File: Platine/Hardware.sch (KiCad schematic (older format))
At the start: 163 parts, among them J1 Barrel_Jack_Switch, J2 Screw_Terminal_01x02, J3 USB_B, Q1 BCX19, Q2 BCX19, SW1 SW_Soft_Reset, SW2 SW_Hard_Reset, SW3 SW_Flash, U1 ESP32-WROOM-32D, U2 ZLDO1117_SOT223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

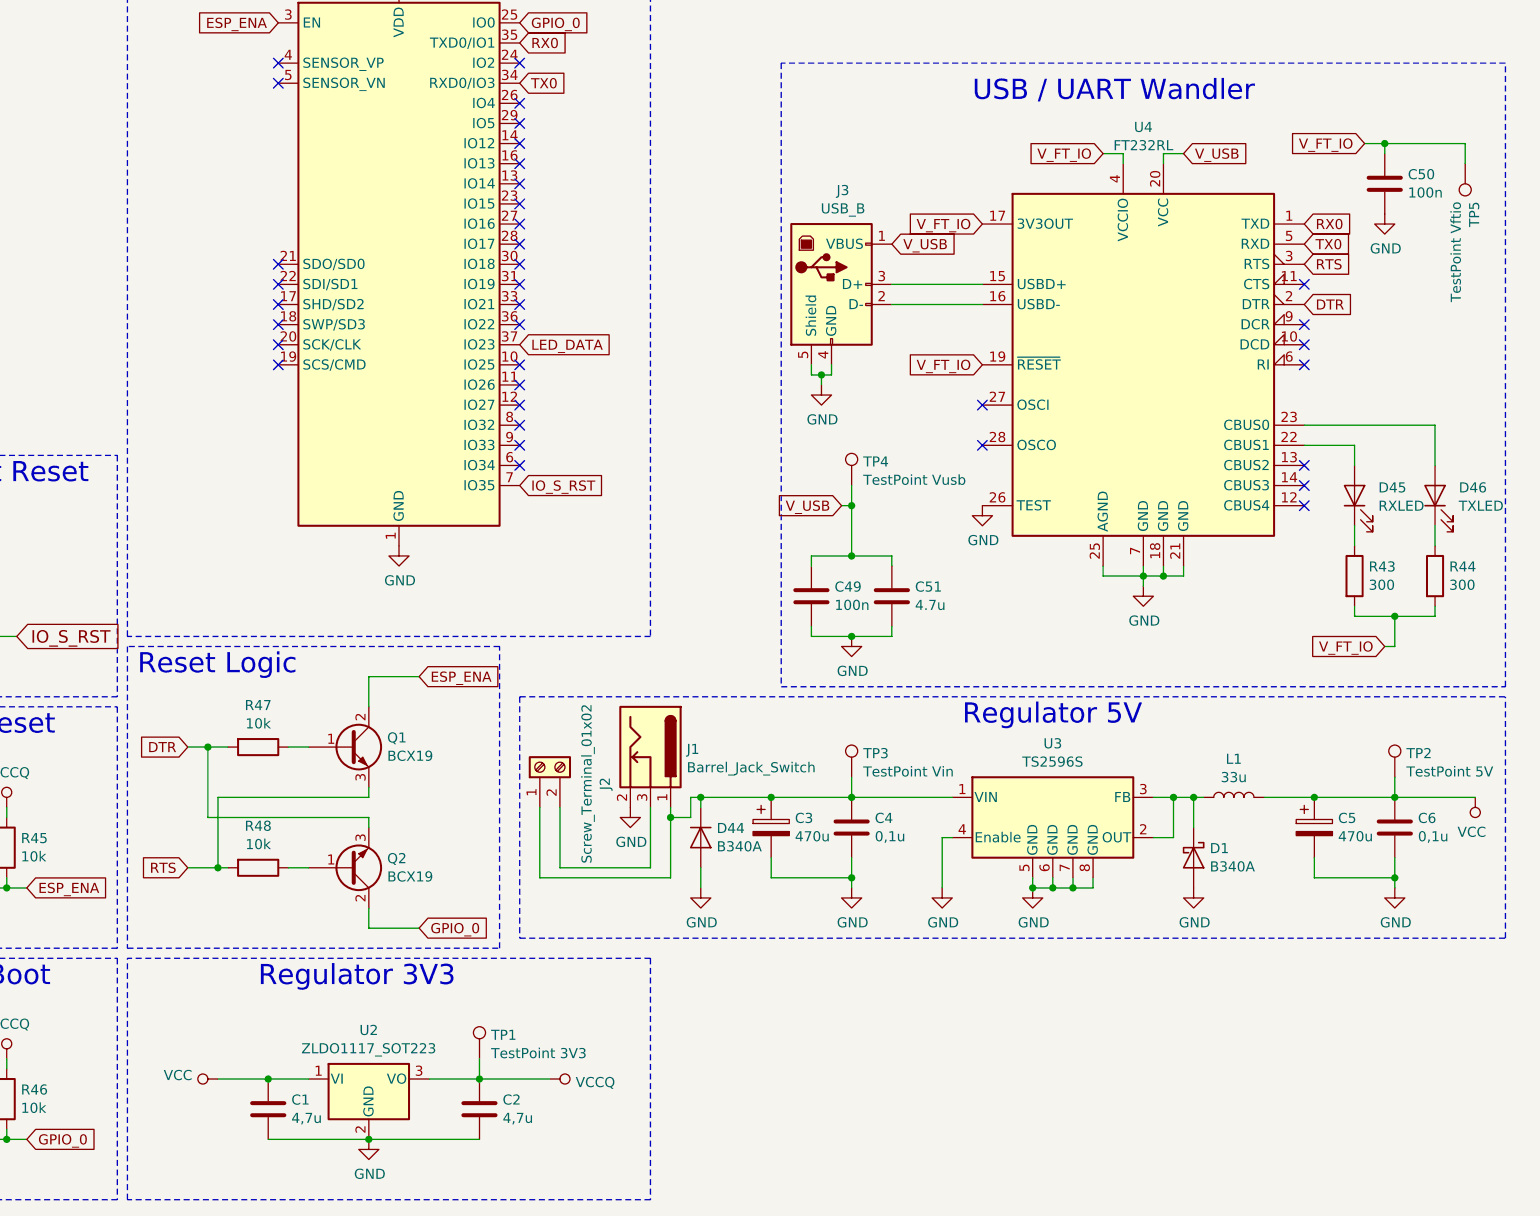
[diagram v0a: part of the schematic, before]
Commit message: Added urgent features requested by client Added power LED Added option to supply complete PCB via USB port
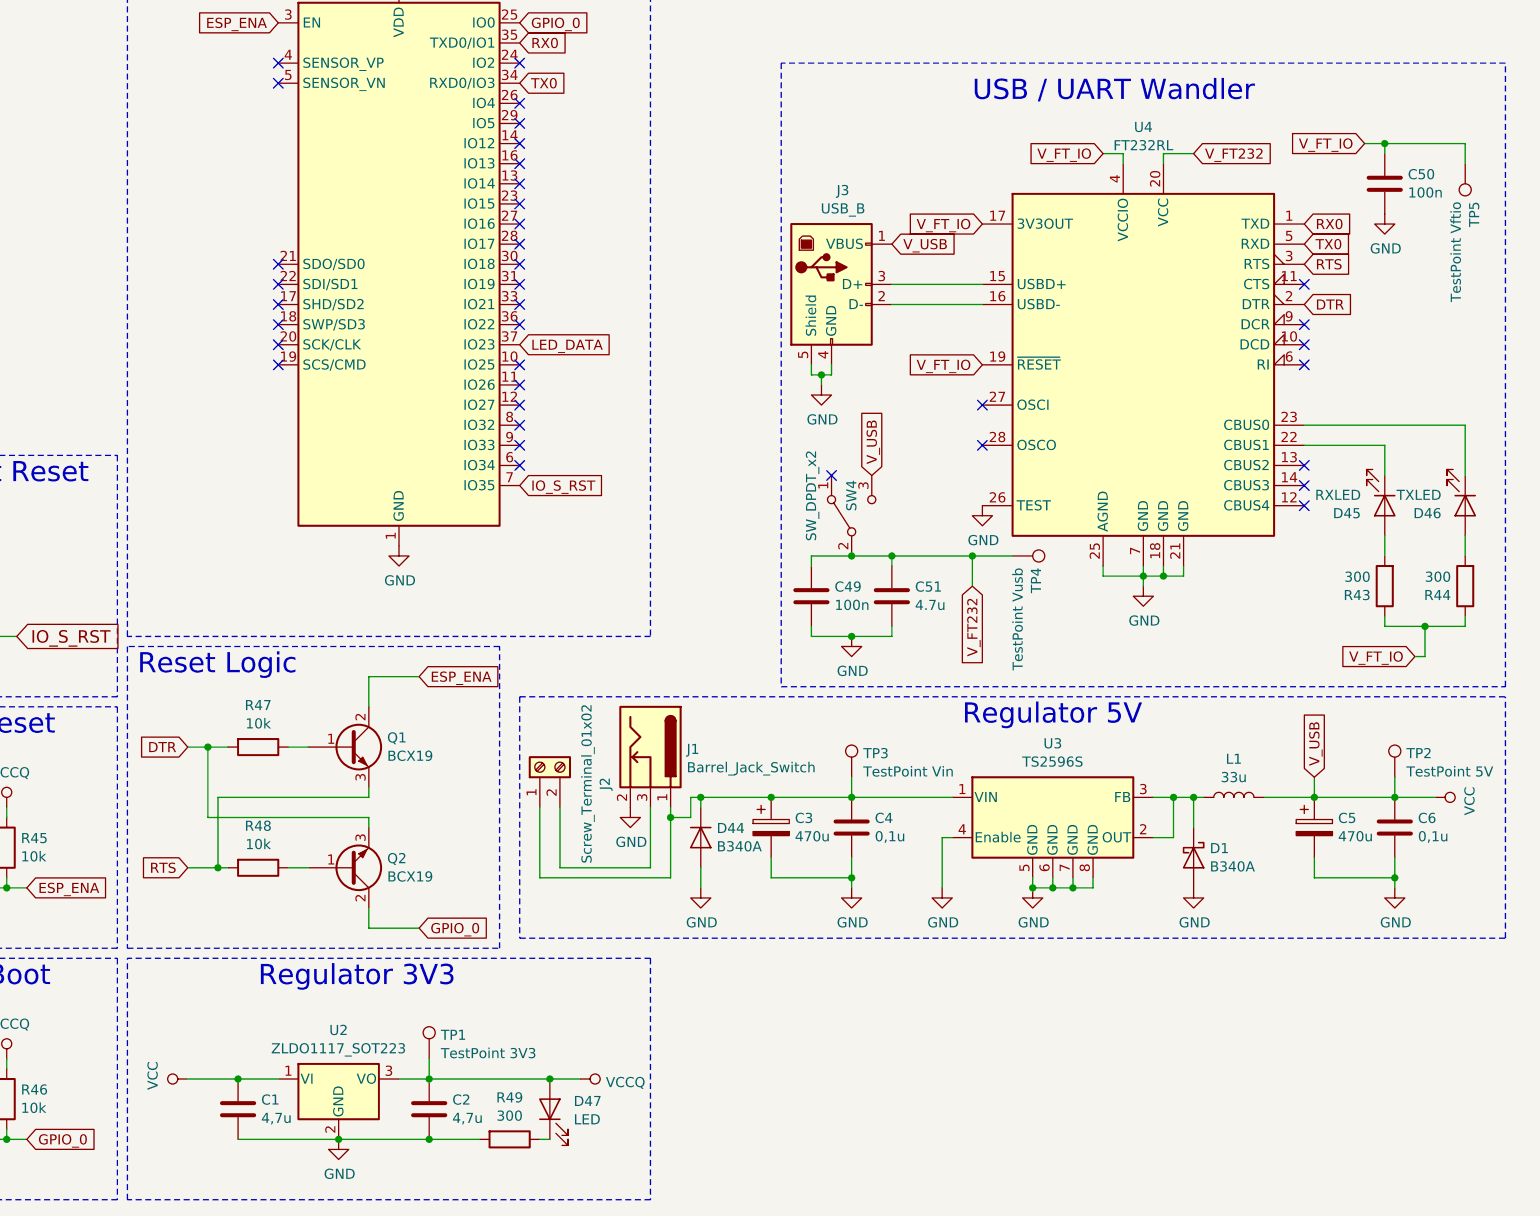
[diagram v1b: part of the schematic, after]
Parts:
- added D47: LED, Diode_SMD:D_0805_2012Metric_Pad1.15x1.40mm_HandSolder, symbol Device:LED
- added R49: 300, Resistor_SMD:R_0805_2012Metric_Pad1.15x1.40mm_HandSolder, symbol Device:R
- added SW4: SW_DPDT_x2, Custom_Footprints:Switch, symbol Switch:SW_SPDT
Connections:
- net GND: now also R49.2
- net VCC: now also J3.1 (VBUS), SW4.3 (C)
- net VCCQ: now also D47.2 (A)
- net V_FT_IO: now also R43.1, R44.1; no longer R43.2, R44.2
- net at U4.22 (CBUS1): now also D45.1 (K); no longer D45.2 (A)
- net at U4.23 (CBUS0): now also D46.1 (K); no longer D46.2 (A)
- net V_USB renamed V_FT232
- net V_FT232: now also SW4.2 (B); no longer J3.1 (VBUS)
- new net: D47.1 (K), R49.1
- new net: D45.2 (A), R43.2
- new net: D46.2 (A), R44.2
- no-connect marks 37 -> 38
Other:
- moved on the sheet: C1, C2, D45, D46, R43, R44, TP1, TP4, U2

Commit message: Production readiness Improved reverse USB powerprotection Added part orderlist
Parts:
- added Q3: NDS0610, Package_TO_SOT_SMD:SOT-23, symbol Transistor_FET:VP0610T
- added R50, R51: 10k, Resistor_SMD:R_0805_2012Metric_Pad1.15x1.40mm_HandSolder, symbol Device:R
- added U5: OP07, Package_SO:SO-8_5.3x6.2mm_P1.27mm, symbol Amplifier_Operational:OP07
- D47: footprint Diode_SMD:D_0805_2012Metric_Pad1.15x1.40mm_HandSolder -> LED_SMD:LED_0805_2012Metric_Pad1.15x1.40mm_HandSolder
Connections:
- net GND: now also R51.2, U5.4 (V-)
- net VCC: now also Q3.2 (S), U5.7 (V+); no longer J3.1 (VBUS), SW4.3 (C)
- net VCCQ: now also U5.2 (-)
- net V_IN: now reaches C3.1, C4.1, D44.1 (K), J1.1, J2.1 (Pin_1), TP3.1, U3.1 (VIN)
- net V_IN: now also R50.1
- new net: R50.2, R51.1, U5.3 (+)
- new net: Q3.1 (G), U5.6
- new net V_USB: J3.1 (VBUS), Q3.3 (D), SW4.3 (C)
- no-connect marks 38 -> 40
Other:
- note added: "USB power protection"
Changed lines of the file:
@@
 	1    0    0    -1
 $EndComp
-Wire Wire Line
-	12950 6650 13400 6650
-Wire Wire Line
-	12950 6750 13400 6750
 Text GLabel 15000 6450 2    50   Input ~ 0
 TX0
@@
 Text GLabel 12950 6450 2    50   Input ~ 0
 V_USB
-Text GLabel 14450 6000 2    50   Input ~ 0
-V_FT232
 Wire Wire Line
 	14300 6000 14300 6050
@@
 F 0 "D47" V 11289 10632 50  0000 R CNN
 F 1 "LED" V 11198 10632 50  0000 R CNN
-F 2 "Diode_SMD:D_0805_2012Metric_Pad1.15x1.40mm_HandSolder" H 11250 10750 50  0001 C CNN
+F 2 "LED_SMD:LED_0805_2012Metric_Pad1.15x1.40mm_HandSolder" H 11250 10750 50  0001 C CNN
 F 3 "https://cdn-reichelt.de/documents/datenblatt/A500/17_21SYGC_S530_E2_TR8_ENG_DATASHEET.pdf" H 11250 10750 50  0001 C CNN
 	1    11250 10750
@@
 	0    -1   -1   0
 $EndComp
-Wire Wire Line
-	15050 9200 15050 9100
-Text GLabel 15050 9100 1    50   Input ~ 0
+NoConn ~ 14150 4950
+NoConn ~ 14250 4950
+Text GLabel 11450 9750 2    50   Input ~ 0
+V_IN
+Wire Wire Line
+	11450 9750 11200 9750
+Wire Wire Line
+	11200 9750 11200 9600
+Connection ~ 11200 9600
+Text GLabel 13350 3950 0    50   Input ~ 0
+V_IN
+$Comp
+L Device:R R50
+U 1 1 6007B0D4
+P 13500 4350
+F 0 "R50" H 13570 4396 50  0000 L CNN
+F 1 "10k" H 13570 4305 50  0000 L CNN
+F 2 "Resistor_SMD:R_0805_2012Metric_Pad1.15x1.40mm_HandSolder" V 13430 4350 50  0001 C CNN
+F 3 "~" H 13500 4350 50  0001 C CNN
+	1    13500 4350
+	1    0    0    -1
+$EndComp
+$Comp
+L Device:R R51
+U 1 1 6007C91D
+P 13500 4750
+F 0 "R51" H 13570 4796 50  0000 L CNN
+F 1 "10k" H 13570 4705 50  0000 L CNN
+F 2 "Resistor_SMD:R_0805_2012Metric_Pad1.15x1.40mm_HandSolder" V 13430 4750 50  0001 C CNN
+F 3 "~" H 13500 4750 50  0001 C CNN
+	1    13500 4750
+	1    0    0    -1
+$EndComp
+$Comp
+L power:GND #PWR?
+U 1 1 6007E1F7
+P 13500 5250
+F 0 "#PWR?" H 13500 5000 50  0001 C CNN
+F 1 "GND" H 13505 5077 50  0000 C CNN
+F 2 "" H 13500 5250 50  0001 C CNN
+F 3 "" H 13500 5250 50  0001 C CNN
+	1    13500 5250
+	1    0    0    -1
+$EndComp
+$Comp
+L Amplifier_Operational:OP07 U5
+U 1 1 5FDF6D96
+P 14150 4650
+F 0 "U5" H 14494 4696 50  0000 L CNN
+F 1 "OP07" H 14494 4605 50  0000 L CNN
+F 2 "Package_SO:SO-8_5.3x6.2mm_P1.27mm" H 14200 4700 50  0001 C CNN
+F 3 "https://www.analog.com/media/en/technical-documentation/data-sheets/OP07.pdf" H 14200 4800 50  0001 C CNN
+	1    14150 4650
+	1    0    0    -1
+$EndComp
+Wire Wire Line
+	14050 4950 14050 5150
+Wire Wire Line
+	14050 5150 13500 5150
+Connection ~ 13500 5150
+Wire Wire Line
+	13500 5150 13500 5250
+Wire Wire Line
+	13500 4200 13500 3950
+Wire Wire Line
+	13500 3950 13350 3950
+Wire Wire Line
+	13500 4500 13500 4550
+Wire Wire Line
+	13850 4550 13500 4550
+Connection ~ 13500 4550
+Wire Wire Line
+	13500 4550 13500 4600
+Wire Wire Line
+	13500 4900 13500 5150
+$Comp
+L power:VCCQ #PWR?
+U 1 1 606D521E
+P 13800 4850
+F 0 "#PWR?" H 13800 4700 50  0001 C CNN
+F 1 "VCCQ" H 13818 5023 50  0000 C CNN
+F 2 "" H 13800 4850 50  0001 C CNN
+F 3 "" H 13800 4850 50  0001 C CNN
+	1    13800 4850
+	-1   0    0    1
+$EndComp
+Wire Wire Line
+	13800 4850 13800 4750
+Wire Wire Line
+	13800 4750 13850 4750
+$Comp
+L power:VCC #PWR?
+U 1 1 60745DA1
+P 14050 4350
+F 0 "#PWR?" H 14050 4200 50  0001 C CNN
+F 1 "VCC" H 14067 4523 50  0000 C CNN
+F 2 "" H 14050 4350 50  0001 C CNN
+F 3 "" H 14050 4350 50  0001 C CNN
+	1    14050 4350
+	1    0    0    -1
+$EndComp
+$Comp
+L Transistor_FET:VP0610T Q3
+U 1 1 609171B8
+P 14900 4650
+F 0 "Q3" H 15104 4696 50  0000 L CNN
+F 1 "NDS0610" H 15104 4605 50  0000 L CNN
+F 2 "Package_TO_SOT_SMD:SOT-23" H 15100 4575 50  0001 L CIN
+F 3 "http://www.vishay.com/docs/70209/70209.pdf" H 14900 4650 50  0001 L CNN
+	1    14900 4650
+	1    0    0    -1
+$EndComp
+Wire Wire Line
+	14700 4650 14450 4650
+Wire Wire Line
+	12950 6750 13400 6750
+Wire Wire Line
+	12950 6650 13400 6650
+Text GLabel 14950 4300 0    50   Input ~ 0
 V_USB
+Wire Wire Line
+	14950 4300 15000 4300
+Wire Wire Line
+	15000 4300 15000 4450
+Wire Wire Line
+	15000 4850 15000 4950
+Wire Wire Line
+	15000 4950 14950 4950
+$Comp
+L power:VCC #PWR?
+U 1 1 60C2B3F3
+P 14950 4950
+F 0 "#PWR?" H 14950 4800 50  0001 C CNN
+F 1 "VCC" V 14968 5077 50  0000 L CNN
+F 2 "" H 14950 4950 50  0001 C CNN
+F 3 "" H 14950 4950 50  0001 C CNN
+	1    14950 4950
+	0    -1   -1   0
+$EndComp
+Text GLabel 14450 6000 2    50   Input ~ 0
+V_FT232
+Wire Notes Line
+	12400 5500 16000 5500
+Wire Notes Line
+	16000 5500 16000 3450
+Wire Notes Line
+	16000 3450 12400 3450
+Wire Notes Line
+	12400 3450 12400 5500
+Text Notes 13500 3700 0    100  ~ 0
+USB power protection
 $EndSCHEMATC

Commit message: Fixed RX & TX Issue #5 Switched RX & TX of FT232RL and ESP 32.
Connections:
- net RX0: now also U4.5 (RXD); no longer U4.1 (TXD)
- net TX0: now also U4.1 (TXD); no longer U4.5 (RXD)
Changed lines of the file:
@@
 	1    0    0    -1
 $EndComp
+Text GLabel 15000 6350 2    50   Input ~ 0
+TX0
 Text GLabel 15000 6450 2    50   Input ~ 0
-TX0
-Text GLabel 15000 6350 2    50   Input ~ 0
 RX0
 Text GLabel 11100 5650 2    50   Input ~ 0

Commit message: Resolved Issue 6 & Issue 7 Switched Pin 2 & 3 of P-FET (Issue 6) Upgraded P-FET to handle 2A continuous (Issue 7)
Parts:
- removed Q3: NDS0610, Package_TO_SOT_SMD:SOT-23, symbol Transistor_FET:VP0610T
- added Q3: DMP3098L7, Package_TO_SOT_SMD:SOT-23, symbol Custom_Symbols:DMP3098L7
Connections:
- net VCC: now also Q3.3 (Drain)
- net V_USB: now also Q3.2 (Source)
- net at U5.6: now also Q3.1 (Gate)
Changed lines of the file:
@@
-	1    0    0    -1
-$EndComp
-$Comp
-L Transistor_FET:VP0610T Q3
-U 1 1 609171B8
-P 14900 4650
-F 0 "Q3" H 15104 4696 50  0000 L CNN
-F 1 "NDS0610" H 15104 4605 50  0000 L CNN
-F 2 "Package_TO_SOT_SMD:SOT-23" H 15100 4575 50  0001 L CIN
-F 3 "http://www.vishay.com/docs/70209/70209.pdf" H 14900 4650 50  0001 L CNN
-	1    14900 4650
 	1    0    0    -1
 $EndComp
@@
 Wire Wire Line
 	12950 6650 13400 6650
-Text GLabel 14950 4300 0    50   Input ~ 0
+Text GLabel 14950 4950 0    50   Input ~ 0
 V_USB
 Wire Wire Line
@@
 L power:VCC #PWR?
 U 1 1 60C2B3F3
-P 14950 4950
-F 0 "#PWR?" H 14950 4800 50  0001 C CNN
-F 1 "VCC" V 14968 5077 50  0000 L CNN
-F 2 "" H 14950 4950 50  0001 C CNN
-F 3 "" H 14950 4950 50  0001 C CNN
-	1    14950 4950
+P 14950 4300
+F 0 "#PWR?" H 14950 4150 50  0001 C CNN
+F 1 "VCC" V 14968 4427 50  0000 L CNN
+F 2 "" H 14950 4300 50  0001 C CNN
+F 3 "" H 14950 4300 50  0001 C CNN
+	1    14950 4300
 	0    -1   -1   0
 $EndComp
@@
 Text Notes 13500 3700 0    100  ~ 0
 USB power protection
+$Comp
+L Custom_Symbols:DMP3098L7 Q3
+U 1 1 60451DB9
+P 14900 4650
+F 0 "Q3" H 15104 4696 50  0000 L CNN
+F 1 "DMP3098L7" H 15104 4605 50  0000 L CNN
+F 2 "Package_TO_SOT_SMD:SOT-23" H 15100 4575 50  0001 L CIN
+F 3 "https://cdn-reichelt.de/documents/datenblatt/A200/ZETEX_DMP3098L_ENG_TDS.pdf" V 14900 4650 50  0001 L CNN
+	1    14900 4650
+	1    0    0    -1
+$EndComp
 $EndSCHEMATC

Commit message: Rerouted feedbackline. close #4 Rerouted to after smoothing coil
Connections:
- net VCC: now also U3.3 (FB)
- net at D1.1 (K), L1.1, U3.2 (OUT): no longer U3.3 (FB)
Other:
- moved on the sheet: C5, C6, L1, TP2
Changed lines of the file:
@@
 L Device:L L1
 U 1 1 5FB4650F
-P 14650 9200
-F 0 "L1" V 14840 9200 50  0000 C CNN
-F 1 "33u" V 14749 9200 50  0000 C CNN
-F 2 "Inductor_SMD:L_10.4x10.4_H4.8" H 14650 9200 50  0001 C CNN
-F 3 "https://cdn-reichelt.de/documents/datenblatt/B400/PIHV4119.pdf" H 14650 9200 50  0001 C CNN
-	1    14650 9200
+P 14650 9300
+F 0 "L1" V 14840 9300 50  0000 C TNN
+F 1 "33u" V 14749 9300 50  0000 C TNN
+F 2 "Inductor_SMD:L_10.4x10.4_H4.8" H 14650 9300 50  0001 C CNN
+F 3 "https://cdn-reichelt.de/documents/datenblatt/B400/PIHV4119.pdf" H 14650 9300 50  0001 C CNN
+	1    14650 9300
 	0    -1   -1   0
 $EndComp
@@
 Connection ~ 13650 9650
 Wire Wire Line
-	14250 9200 14350 9200
-Wire Wire Line
 	14250 9400 14350 9400
-Wire Wire Line
-	14350 9400 14350 9200
-Connection ~ 14350 9200
-Wire Wire Line
-	14350 9200 14450 9200
 $Comp
 L Device:CP C5
 U 1 1 5FB4F73A
-P 15050 9350
-F 0 "C5" H 15168 9396 50  0000 L CNN
-F 1 "470u" H 15168 9305 50  0000 L CNN
-F 2 "Capacitor_SMD:CP_Elec_6.3x7.7" H 15088 9200 50  0001 C CNN
-F 3 "https://cdn-reichelt.de/documents/datenblatt/B300/ABA0000C34.pdf" H 15050 9350 50  0001 C CNN
-	1    15050 9350
+P 15050 9450
+F 0 "C5" H 15168 9496 50  0000 L CNN
+F 1 "470u" H 15168 9405 50  0000 L CNN
+F 2 "Capacitor_SMD:CP_Elec_6.3x7.7" H 15088 9300 50  0001 C CNN
+F 3 "https://cdn-reichelt.de/documents/datenblatt/B300/ABA0000C34.pdf" H 15050 9450 50  0001 C CNN
+	1    15050 9450
 	1    0    0    -1
 $EndComp
@@
 L Device:C C6
 U 1 1 5FB4F740
-P 15450 9350
-F 0 "C6" H 15565 9396 50  0000 L CNN
-F 1 "0,1u" H 15565 9305 50  0000 L CNN
-F 2 "Capacitor_SMD:C_0805_2012Metric_Pad1.15x1.40mm_HandSolder" H 15488 9200 50  0001 C CNN
-F 3 "https://cdn-reichelt.de/documents/datenblatt/B300/KEM_C0XXX_C0G_DB-EN.pdf" H 15450 9350 50  0001 C CNN
-	1    15450 9350
+P 15450 9450
+F 0 "C6" H 15565 9496 50  0000 L CNN
+F 1 "0,1u" H 15565 9405 50  0000 L CNN
+F 2 "Capacitor_SMD:C_0805_2012Metric_Pad1.15x1.40mm_HandSolder" H 15488 9300 50  0001 C CNN
+F 3 "https://cdn-reichelt.de/documents/datenblatt/B300/KEM_C0XXX_C0G_DB-EN.pdf" H 15450 9450 50  0001 C CNN
+	1    15450 9450
 	1    0    0    -1
 $EndComp
-Wire Wire Line
-	15050 9500 15050 9600
 $Comp
 L power:GND #PWR0110
@@
 	1    0    0    -1
 $EndComp
-Wire Wire Line
-	14450 9350 14450 9200
-Connection ~ 14450 9200
-Wire Wire Line
-	14450 9200 14500 9200
 $Comp
 L Device:D_Schottky D1
@@
 Wire Wire Line
 	12750 9600 12750 9650
-Connection ~ 15450 9200
+Connection ~ 15450 9300
 Wire Wire Line
-	15050 9200 15450 9200
-Wire Wire Line
-	15450 9500 15450 9600
+	15050 9300 15450 9300
 Wire Wire Line
 	15050 9600 15450 9600
-Connection ~ 15450 9600
 Wire Wire Line
 	15450 9600 15450 9650
@@
 L Connector:TestPoint TP2
 U 1 1 605C9295
-P 15450 9100
-F 0 "TP2" H 15508 9218 50  0000 L CNN
-F 1 "TestPoint 5V" H 15508 9127 50  0000 L CNN
-F 2 "TestPoint:TestPoint_Pad_D2.0mm" H 15650 9100 50  0001 C CNN
-F 3 "~" H 15650 9100 50  0001 C CNN
-	1    15450 9100
+P 15450 9200
+F 0 "TP2" H 15508 9318 50  0000 L CNN
+F 1 "TestPoint 5V" H 15508 9227 50  0000 L CNN
+F 2 "TestPoint:TestPoint_Pad_D2.0mm" H 15650 9200 50  0001 C CNN
+F 3 "~" H 15650 9200 50  0001 C CNN
+	1    15450 9200
 	1    0    0    -1
 $EndComp
 Wire Wire Line
-	15450 9100 15450 9200
+	15450 9200 15450 9300
 $Comp
 L Connector:TestPoint TP3
@@
 L power:VCC #PWR0105
 U 1 1 6324EB30
-P 15650 9200
-F 0 "#PWR0105" H 15650 9050 50  0001 C CNN
-F 1 "VCC" H 15668 9373 50  0000 C CNN
-F 2 "" H 15650 9200 50  0001 C CNN
-F 3 "" H 15650 9200 50  0001 C CNN
-	1    15650 9200
+P 15650 9300
+F 0 "#PWR0105" H 15650 9150 50  0001 C CNN
+F 1 "VCC" H 15668 9473 50  0000 C CNN
+F 2 "" H 15650 9300 50  0001 C CNN
+F 3 "" H 15650 9300 50  0001 C CNN
+	1    15650 9300
 	0    1    1    0
 $EndComp
 Wire Wire Line
-	15650 9200 15450 9200
+	15650 9300 15450 9300
 Wire Wire Line
-	14800 9200 15050 9200
-Connection ~ 15050 9200
+	14800 9300 15050 9300
+Connection ~ 15050 9300
 $Comp
 L power:VCC #PWR0111
@@
 	1    0    0    -1
 $EndComp
+Connection ~ 15450 9600
+Wire Wire Line
+	14350 9400 14350 9300
+Wire Wire Line
+	14350 9300 14450 9300
+Wire Wire Line
+	14450 9350 14450 9300
+Connection ~ 14450 9300
+Wire Wire Line
+	14450 9300 14500 9300
+Wire Wire Line
+	14250 9200 15050 9200
+Wire Wire Line
+	15050 9200 15050 9300
 $EndSCHEMATC
